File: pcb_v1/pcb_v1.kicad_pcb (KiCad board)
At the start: 2 copper layers, 28 x 53 mm, 38 parts, among them J1 Conn_02x03_Odd_Even, J2 Conn_01x02, J3 Conn_01x04, J4 Conn_01x07, U1 tmp117, U2 tmp117, U3 tmp117, U4 tmp117, U5 TC78H651AFNG,EL_Dual_H-Bridge, U6 STM32L432KBUx, Y1 Crystal

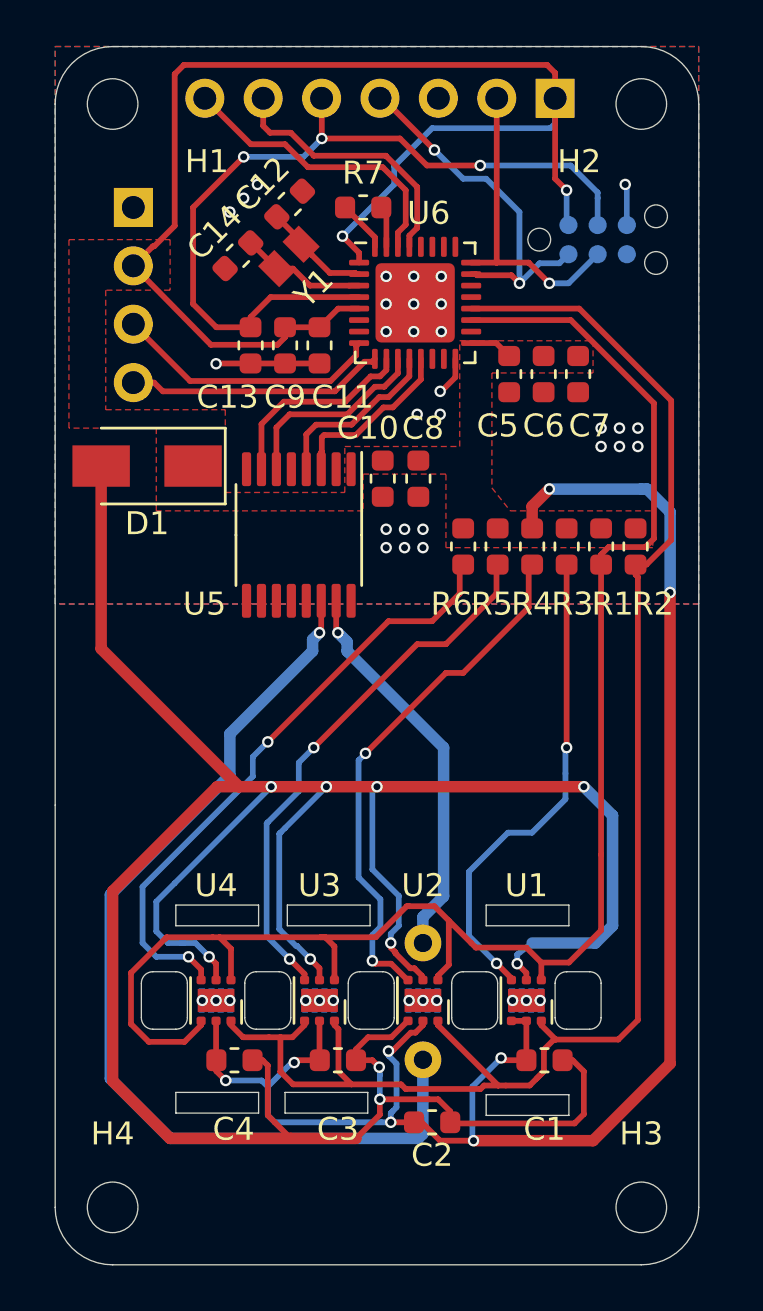
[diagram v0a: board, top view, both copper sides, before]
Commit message: Updated PCB w extra position
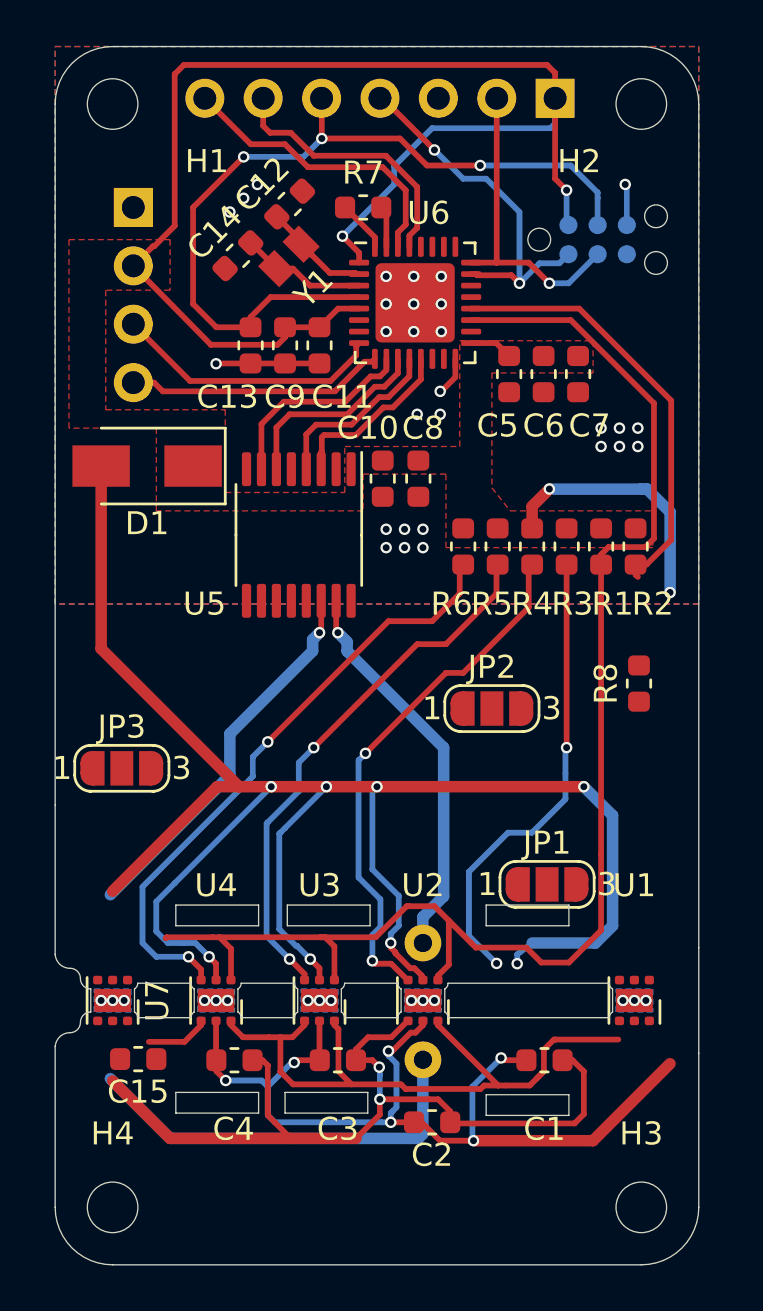
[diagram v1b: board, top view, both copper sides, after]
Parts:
- added C15: 100nF, Capacitor_SMD:C_0603_1608Metric, F.Cu at (162.6, 124.0)
- added JP1: SolderJumper_3_Open, Jumper:SolderJumper-3_P1.3mm_Open_RoundedPad1.0x1.5mm_NumberLabels, F.Cu at (180.4, 116.5)
- added JP2: SolderJumper_3_Open, Jumper:SolderJumper-3_P1.3mm_Open_RoundedPad1.0x1.5mm_NumberLabels, F.Cu at (178.0, 108.8)
- added JP3: SolderJumper_3_Open, Jumper:SolderJumper-3_P1.3mm_Open_RoundedPad1.0x1.5mm_NumberLabels, F.Cu at (161.9, 111.4)
- added R8: 10k, Capacitor_SMD:C_0603_1608Metric, F.Cu at (184.4, 107.7)
- added U7: tmp117, Package_SON:WSON-6-1EP_2x2mm_P0.65mm_EP1x1.6mm, F.Cu at (161.5, 121.5)
- moved U1 4.70 mm to (184.2, 121.5)
- moved G*** 0.50 mm to (163.1, 100.3)
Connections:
- net /OUT1 renamed Net-(U5-Pad12)
- net /OUT2 renamed Net-(U5-Pad11)
- U3 pad 4: /SDA -> /ADD1
- U4 pad 4: /SCL -> /ADD2
- U5 pad 6: /PA5 -> Net-(U5-Pad6)
- U5 pad 7: /PA4 -> Net-(U5-Pad7)
- U6 pad 10: /PA4 -> Net-(U6-Pad10)
- U6 pad 11: /PA5 -> Net-(U6-Pad11)
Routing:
- net VDD: track 135.8 -> 113.0 mm
- net /SDA: track 69.8 -> 48.3 mm
- net GND: track 138.6 -> 129.4 mm
- net /SCL: track 71.6 -> 62.7 mm
- net /OUT3: track 42.6 -> 34.6 mm
- net /ADD2: track 0.00 -> 2.76 mm
- net Net-(R3-Pad1): track 21.3 -> 20.3 mm
- net Net-(U7-Pad7): vias 0 -> 3
- added copper zone on B.Cu, net Net-(U7-Pad7)
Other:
- outline, holes or cut-outs redrawn
- board text added: "A - 1.5mm B - 1.9mm C - 2.6mm"
- board text added: "Manufacturing Requirements 1. Thin PCB thickness (0.3mm), 10% tolerance 2. FR4 135tg-310td laminate 3. Copper 1 oz 4. ENIG-RoHS finish as per IPC-4552 5. Green solder mask 6. White silkscreen 7. No silkscreen allowed on component pads 8. Eco1.User polygon should be filled with conductive material 9. Eco2.User polygon denotes where IPC Standard Hard Gold Finish is applied 10. Cu to Board Edge - Ro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"
- board text added: "Special Order: 1. Conductively-Filled Vias 2. Thin PCB (0.3 mm) 3. Hard Gold Finish 4. Routed Edges (0.15mm)"
- board text removed: "A - 1.5mm B - 2.5mm C - 2.0mm"
- board text removed: "Manufacturing Requirements 1. Thin PCB thickness (0.3mm), 10% tolerance 2. FR4 135tg-310td laminate 3. Copper 1 oz 4. ENIG-RoHS finish as per IPC-4552 5. Green solder mask 6. White silkscreen 7. No silkscreen allowed on component pads 8. Eco1.User polygon should be filled with conductive material 9. Eco2.User polygon denotes where IPC Standard Hard Gold Finish is applied"
- board text removed: "Special Order: 1. Conductively-Filled Vias 2. 0.3mm Thick PCB 3. Hard Gold Finish"

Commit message: updated PCB files
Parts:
- U1, U2, U3, U4, U7: footprint Package_SON:WSON-6-1EP_2x2mm_P0.65mm_EP1x1.6mm -> flowsensor:THERMAL_ENHANCED_WSON-6-1EP_2x2mm_P0.65mm_EP1x1.6mm
- moved JP2 22.5 mm to (173.0, 130.8)
- moved JP3 20.0 mm to (167.0, 130.8)
- moved JP1 14.4 mm to (179.0, 130.8)
- moved R8 10.9 mm to (175.0, 102.2)
- moved H2 0.75 mm to (185.2, 82.5)
- moved H3 0.75 mm to (185.2, 130.5)
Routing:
- net /SDA: track 48.3 -> 109.2 mm, vias 0 -> 5
- net VDD: track 113.0 -> 153.1 mm, vias 10 -> 11
- net /SCL: track 62.7 -> 102.3 mm, vias 0 -> 2
- net Net-(R8-Pad1): track 0.00 -> 24.1 mm, vias 0 -> 2
- net /OUT3: track 34.6 -> 52.4 mm
- net GND: track 129.4 -> 147.0 mm, vias 39 -> 38
- net /ADD1: track 0.00 -> 17.6 mm, vias 0 -> 2
- net /ADD2: track 2.76 -> 16.5 mm, vias 0 -> 2
- net /ADD3: track 0.00 -> 12.2 mm
- net /PA4: track 8.86 -> 0.00 mm
- net /PA5: track 8.70 -> 0.00 mm
- net Net-(R3-Pad1): track 20.3 -> 26.0 mm
- net Net-(R6-Pad1): track 26.8 -> 26.2 mm
- net Net-(U7-Pad7): vias 3 -> 6
- net Net-(U4-Pad7): vias 3 -> 6
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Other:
- board size 28 x 53 mm -> 28.8 x 53 mm
- net class via added: clearance 0.075, trace_width 0.25, via_dia 0.4, via_drill 0.3
- board text added: "Manufacturing Requirements 1. Thin PCB thickness (0.3mm), 10% tolerance 2. FR4 135tg-310td laminate 3. Copper 1/2 oz 4. ENIG-RoHS finish as per IPC-4552 5. Green solder mask 6. White silkscreen 7. No silkscreen allowed on component pads 8. Eco1.User polygon covers vias which should be filled with thermally conductive material 9. Eco2.User polygon denotes where IPC Standard Hard Gold Finish is app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"
- board text removed: "Manufacturing Requirements 1. Thin PCB thickness (0.3mm), 10% tolerance 2. FR4 135tg-310td laminate 3. Copper 1 oz 4. ENIG-RoHS finish as per IPC-4552 5. Green solder mask 6. White silkscreen 7. No silkscreen allowed on component pads 8. Eco1.User polygon should be filled with conductive material 9. Eco2.User polygon denotes where IPC Standard Hard Gold Finish is applied 10. Cu to Board Edge - Ro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"
